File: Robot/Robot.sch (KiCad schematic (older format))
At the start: 29 parts, among them Q1 NPN, U1 MENC, U2 MENC

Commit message: Dodani nekateri elementi na shemi
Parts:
- added C?: C, symbol C
- added D?: LED, symbol LED
- added Q?: Q_PMOS_GDS, symbol Q_PMOS_GDS
- added R? (x3): 10k, symbol R
- added R?: 150, symbol R
- added SW?: SPDT_Switch, symbol SPDT_Switch
- Q1: value NPN -> NPN B=100
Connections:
- net labels added: BATVOL, LEDBAT
- wire segments 166 -> 189
- no-connect marks 12 -> 11
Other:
- note added: "Z LED lučko prikazujemo napetost na bateriji."
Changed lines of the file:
@@
 U 1 1 58BBD1F6
 P 2450 1300
-F 0 "BT1" H 2550 1400 50  0000 L CNN
-F 1 "Baterija 9V" H 2550 1300 50  0000 L CNN
+F 0 "BT1" V 2200 1350 50  0000 L CNN
+F 1 "Baterija 9V" V 2300 1200 50  0000 L CNN
 F 2 "" V 2450 1360 50  0000 C CNN
 F 3 "" V 2450 1360 50  0000 C CNN
@@
 L +9V #PWR3
 U 1 1 58BBD76D
-P 2450 1100
-F 0 "#PWR3" H 2450 950 50  0001 C CNN
-F 1 "+9V" H 2450 1240 50  0000 C CNN
-F 2 "" H 2450 1100 50  0000 C CNN
-F 3 "" H 2450 1100 50  0000 C CNN
-	1    2450 1100
+P 2450 1000
+F 0 "#PWR3" H 2450 850 50  0001 C CNN
+F 1 "+9V" H 2450 1140 50  0000 C CNN
+F 2 "" H 2450 1000 50  0000 C CNN
+F 3 "" H 2450 1000 50  0000 C CNN
+	1    2450 1000
 	1    0    0    -1
 $EndComp
@@
 L GND #PWR4
 U 1 1 58BC083D
-P 2450 1400
-F 0 "#PWR4" H 2450 1150 50  0001 C CNN
-F 1 "GND" H 2450 1250 50  0000 C CNN
-F 2 "" H 2450 1400 50  0000 C CNN
-F 3 "" H 2450 1400 50  0000 C CNN
-	1    2450 1400
+P 2450 1750
+F 0 "#PWR4" H 2450 1500 50  0001 C CNN
+F 1 "GND" H 2450 1600 50  0000 C CNN
+F 2 "" H 2450 1750 50  0000 C CNN
+F 3 "" H 2450 1750 50  0000 C CNN
+	1    2450 1750
 	1    0    0    -1
 $EndComp
@@
 P 4250 8900
 F 0 "Q1" H 4450 8950 50  0000 L CNN
-F 1 "NPN" H 4450 8850 50  0000 L CNN
+F 1 "NPN B=100" H 4450 8850 50  0000 L CNN
 F 2 "" H 4450 9000 50  0000 C CNN
 F 3 "" H 4250 8900 50  0000 C CNN
@@
 	6300 1750 6400 1850
 NoConn ~ 8950 1950
-NoConn ~ 8950 2050
-NoConn ~ 8950 2150
 Entry Wire Line
 	9950 2750 10050 2850
@@
 Text Label 6600 2050 0    60   ~ 0
 AIN1
-Text Label 6600 1850 0    60   ~ 0
-AIN2
 Text Label 6600 1750 0    60   ~ 0
 AOUTL
@@
 Wire Wire Line
 	8950 2350 9350 2350
+$Comp
+L C C?
+U 1 1 58C5CD2F
+P 2800 1250
+F 0 "C?" H 2825 1350 50  0000 L CNN
+F 1 "C" H 2825 1150 50  0000 L CNN
+F 2 "" H 2838 1100 50  0000 C CNN
+F 3 "" H 2800 1250 50  0000 C CNN
+	1    2800 1250
+	1    0    0    -1
+$EndComp
+Wire Wire Line
+	2450 1100 2450 1000
+Wire Wire Line
+	2450 1400 2450 1750
+Wire Wire Line
+	2800 1400 2450 1400
+NoConn ~ 8950 2550
+Connection ~ 2800 1100
+$Comp
+L R R?
+U 1 1 58C66BFC
+P 4150 1250
+F 0 "R?" V 4230 1250 50  0000 C CNN
+F 1 "10k" V 4150 1250 50  0000 C CNN
+F 2 "" V 4080 1250 50  0000 C CNN
+F 3 "" H 4150 1250 50  0000 C CNN
+	1    4150 1250
+	1    0    0    -1
+$EndComp
+Wire Wire Line
+	2450 1100 4600 1100
+Wire Wire Line
+	3800 1400 4300 1400
+$Comp
+L SPDT_Switch SW?
+U 1 1 58C6748C
+P 3400 1600
+F 0 "SW?" H 3350 1850 60  0000 C CNN
+F 1 "SPDT_Switch" H 3350 1350 60  0000 C CNN
+F 2 "" H 3400 1600 60  0001 C CNN
+F 3 "" H 3400 1600 60  0001 C CNN
+	1    3400 1600
+	1    0    0    -1
+$EndComp
+Wire Wire Line
+	3050 1750 2800 1750
+Wire Wire Line
+	2800 1750 2800 1400
+Wire Wire Line
+	3050 1450 3050 1100
+Connection ~ 3050 1100
+Wire Wire Line
+	3800 1400 3800 1600
+$Comp
+L Q_PMOS_GDS Q?
+U 1 1 58C67B7D
+P 4500 1700
+F 0 "Q?" H 4700 1750 50  0000 L CNN
+F 1 "Q_PMOS_GDS" H 4700 1650 50  0000 L CNN
+F 2 "" H 4700 1800 50  0000 C CNN
+F 3 "" H 4500 1700 50  0000 C CNN
+	1    4500 1700
+	1    0    0    -1
+$EndComp
+Wire Wire Line
+	4300 1400 4300 1700
+Connection ~ 4150 1400
+Wire Wire Line
+	4600 1100 4600 1500
+Connection ~ 4150 1100
+Wire Wire Line
+	4600 1900 4600 2000
+Wire Wire Line
+	4600 2000 5450 2000
+Wire Wire Line
+	5450 2000 5450 1800
+$Comp
+L +9V #PWR?
+U 1 1 58C67FC0
+P 5450 1800
+F 0 "#PWR?" H 5450 1650 50  0001 C CNN
+F 1 "+9V" H 5450 1940 50  0000 C CNN
+F 2 "" H 5450 1800 50  0000 C CNN
+F 3 "" H 5450 1800 50  0000 C CNN
+	1    5450 1800
+	1    0    0    -1
+$EndComp
+$Comp
+L R R?
+U 1 1 58C6804F
+P 5450 2150
+F 0 "R?" V 5530 2150 50  0000 C CNN
+F 1 "10k" V 5450 2150 50  0000 C CNN
+F 2 "" V 5380 2150 50  0000 C CNN
+F 3 "" H 5450 2150 50  0000 C CNN
+	1    5450 2150
+	1    0    0    -1
+$EndComp
+$Comp
+L R R?
+U 1 1 58C680E1
+P 5450 2550
+F 0 "R?" V 5530 2550 50  0000 C CNN
+F 1 "10k" V 5450 2550 50  0000 C CNN
+F 2 "" V 5380 2550 50  0000 C CNN
+F 3 "" H 5450 2550 50  0000 C CNN
+	1    5450 2550
+	1    0    0    -1
+$EndComp
+Wire Wire Line
+	5450 2300 5450 2400
+$Comp
+L GND #PWR?
+U 1 1 58C6828F
+P 5450 2700
+F 0 "#PWR?" H 5450 2450 50  0001 C CNN
+F 1 "GND" H 5450 2550 50  0000 C CNN
+F 2 "" H 5450 2700 50  0000 C CNN
+F 3 "" H 5450 2700 50  0000 C CNN
+	1    5450 2700
+	1    0    0    -1
+$EndComp
+Wire Wire Line
+	5450 2350 4800 2350
+Wire Wire Line
+	4800 2350 4800 3000
+Connection ~ 5450 2350
+Entry Wire Line
+	4800 3000 4900 3100
+Text Label 4950 2350 0    60   ~ 0
+BATVOL
+Wire Wire Line
+	8950 2150 9950 2150
+Entry Wire Line
+	9950 2150 10050 2250
+Text Label 9050 2150 0    60   ~ 0
+BATVOL
+Wire Wire Line
+	8950 2050 9950 2050
+Entry Wire Line
+	9950 2050 10050 2150
+Text Label 9050 2050 0    60   ~ 0
+AIN2
+Text Label 6600 1850 0    60   ~ 0
+LEDBAT
+$Comp
+L LED D?
+U 1 1 58C6B057
+P 11350 1550
+F 0 "D?" H 11350 1650 50  0000 C CNN
+F 1 "LED" H 11350 1450 50  0000 C CNN
+F 2 "" H 11350 1550 50  0000 C CNN
+F 3 "" H 11350 1550 50  0000 C CNN
+	1    11350 1550
+	-1   0    0    1
+$EndComp
+Entry Wire Line
+	10050 1450 10150 1550
+Wire Wire Line
+	10150 1550 11200 1550
+$Comp
+L R R?
+U 1 1 58C6BA8C
+P 11900 1550
+F 0 "R?" V 11980 1550 50  0000 C CNN
+F 1 "150" V 11900 1550 50  0000 C CNN
+F 2 "" V 11830 1550 50  0000 C CNN
+F 3 "" H 11900 1550 50  0000 C CNN
+	1    11900 1550
+	0    1    1    0
+$EndComp
+Wire Wire Line
+	11500 1550 11750 1550
+Wire Wire Line
+	12050 1550 12600 1550
+Wire Wire Line
+	12600 1550 12600 1700
+$Comp
+L GND #PWR?
+U 1 1 58C6BDA7
+P 12600 1700
+F 0 "#PWR?" H 12600 1450 50  0001 C CNN
+F 1 "GND" H 12600 1550 50  0000 C CNN
+F 2 "" H 12600 1700 50  0000 C CNN
+F 3 "" H 12600 1700 50  0000 C CNN
+	1    12600 1700
+	1    0    0    -1
+$EndComp
+Text Label 10450 1550 0    60   ~ 0
+LEDBAT
+Text Notes 11200 1350 0    60   ~ 0
+Z LED lučko prikazujemo napetost na bateriji.
 $EndSCHEMATC

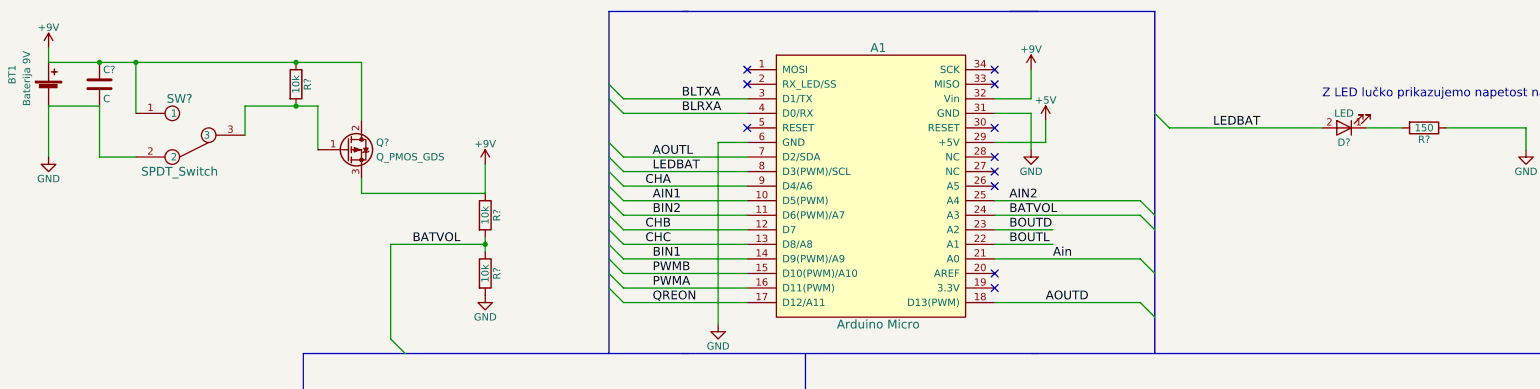
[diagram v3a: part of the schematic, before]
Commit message: Popravljena shema
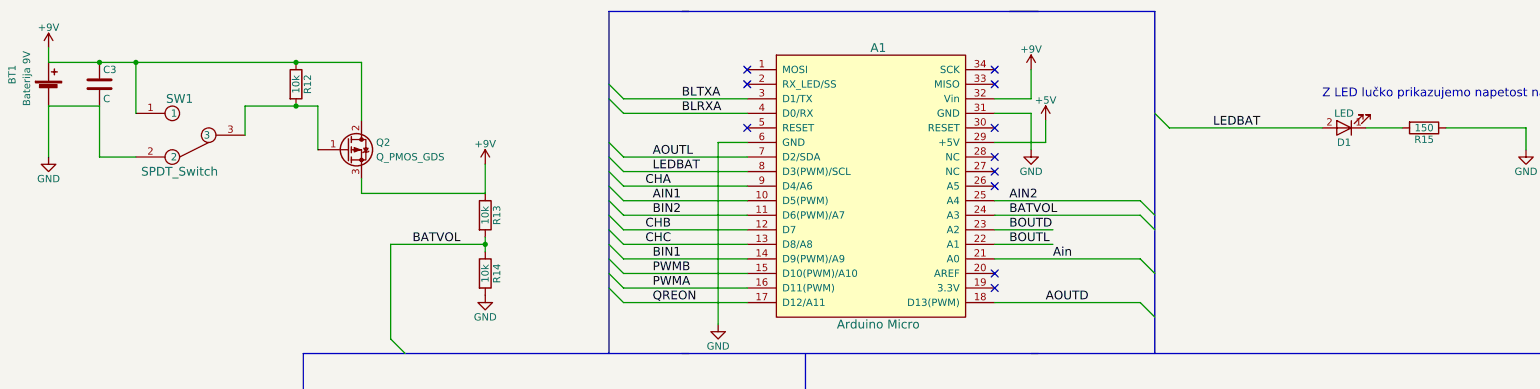
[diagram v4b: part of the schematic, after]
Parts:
- gave numbers to parts that had none: 8
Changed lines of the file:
@@
 $EndComp
 $Comp
-L GND #PWR9
+L GND #PWR11
 U 1 1 58BC1A56
 P 7000 10050
-F 0 "#PWR9" H 7000 9800 50  0001 C CNN
+F 0 "#PWR11" H 7000 9800 50  0001 C CNN
 F 1 "GND" H 7000 9900 50  0000 C CNN
 F 2 "" H 7000 10050 50  0000 C CNN
@@
 $EndComp
 $Comp
-L GND #PWR16
+L GND #PWR18
 U 1 1 58BC1E52
 P 9200 1700
-F 0 "#PWR16" H 9200 1450 50  0001 C CNN
+F 0 "#PWR18" H 9200 1450 50  0001 C CNN
 F 1 "GND" H 9200 1550 50  0000 C CNN
 F 2 "" H 9200 1700 50  0000 C CNN
@@
 $EndComp
 $Comp
-L +9V #PWR15
+L +9V #PWR17
 U 1 1 58BC1EB1
 P 9200 1150
-F 0 "#PWR15" H 9200 1000 50  0001 C CNN
+F 0 "#PWR17" H 9200 1000 50  0001 C CNN
 F 1 "+9V" H 9200 1290 50  0000 C CNN
 F 2 "" H 9200 1150 50  0000 C CNN
@@
 $EndComp
 $Comp
-L +5V #PWR17
+L +5V #PWR19
 U 1 1 58BC1EDB
 P 9300 1500
-F 0 "#PWR17" H 9300 1350 50  0001 C CNN
+F 0 "#PWR19" H 9300 1350 50  0001 C CNN
 F 1 "+5V" H 9300 1640 50  0000 C CNN
 F 2 "" H 9300 1500 50  0000 C CNN
@@
 $EndComp
 $Comp
-L GND #PWR10
+L GND #PWR12
 U 1 1 58BC1F3F
 P 7050 2900
-F 0 "#PWR10" H 7050 2650 50  0001 C CNN
+F 0 "#PWR12" H 7050 2650 50  0001 C CNN
 F 1 "GND" H 7050 2750 50  0000 C CNN
 F 2 "" H 7050 2900 50  0000 C CNN
@@
 $EndComp
 $Comp
-L +5V #PWR11
+L +5V #PWR13
 U 1 1 58BC95B9
 P 7100 4450
-F 0 "#PWR11" H 7100 4300 50  0001 C CNN
+F 0 "#PWR13" H 7100 4300 50  0001 C CNN
 F 1 "+5V" H 7100 4590 50  0000 C CNN
 F 2 "" H 7100 4450 50  0000 C CNN
@@
 $EndComp
 $Comp
-L GND #PWR8
+L GND #PWR10
 U 1 1 58BD222C
 P 6750 7950
-F 0 "#PWR8" H 6750 7700 50  0001 C CNN
+F 0 "#PWR10" H 6750 7700 50  0001 C CNN
 F 1 "GND" H 6750 7800 50  0000 C CNN
 F 2 "" H 6750 7950 50  0000 C CNN
@@
 S4
 $Comp
-L +5V #PWR14
+L +5V #PWR16
 U 1 1 58BD4C14
 P 8300 9100
-F 0 "#PWR14" H 8300 8950 50  0001 C CNN
+F 0 "#PWR16" H 8300 8950 50  0001 C CNN
 F 1 "+5V" H 8300 9240 50  0000 C CNN
 F 2 "" H 8300 9100 50  0000 C CNN
@@
 BLRXA
 $Comp
-L GND #PWR13
+L GND #PWR15
 U 1 1 58BDD562
 P 8150 4350
-F 0 "#PWR13" H 8150 4100 50  0001 C CNN
+F 0 "#PWR15" H 8150 4100 50  0001 C CNN
 F 1 "GND" H 8150 4200 50  0000 C CNN
 F 2 "" H 8150 4350 50  0000 C CNN
@@
 $EndComp
 $Comp
-L +5V #PWR12
+L +5V #PWR14
 U 1 1 58BDD71C
 P 7900 4300
-F 0 "#PWR12" H 7900 4150 50  0001 C CNN
+F 0 "#PWR14" H 7900 4150 50  0001 C CNN
 F 1 "+5V" H 7900 4440 50  0000 C CNN
 F 2 "" H 7900 4300 50  0000 C CNN
@@
 $EndComp
 $Comp
-L +9V #PWR23
+L +9V #PWR26
 U 1 1 58BDF7BA
 P 13250 4400
-F 0 "#PWR23" H 13250 4250 50  0001 C CNN
+F 0 "#PWR26" H 13250 4250 50  0001 C CNN
 F 1 "+9V" H 13250 4540 50  0000 C CNN
 F 2 "" H 13250 4400 50  0000 C CNN
@@
 $EndComp
 $Comp
-L GND #PWR24
+L GND #PWR27
 U 1 1 58BDF8AC
 P 13500 5850
-F 0 "#PWR24" H 13500 5600 50  0001 C CNN
+F 0 "#PWR27" H 13500 5600 50  0001 C CNN
 F 1 "GND" H 13500 5700 50  0000 C CNN
 F 2 "" H 13500 5850 50  0000 C CNN
@@
 $EndComp
 $Comp
-L +5V #PWR20
+L +5V #PWR22
 U 1 1 58BE122F
 P 11000 5500
-F 0 "#PWR20" H 11000 5350 50  0001 C CNN
+F 0 "#PWR22" H 11000 5350 50  0001 C CNN
 F 1 "+5V" H 11000 5640 50  0000 C CNN
 F 2 "" H 11000 5500 50  0000 C CNN
@@
 $EndComp
 $Comp
-L +5V #PWR18
+L +5V #PWR20
 U 1 1 58BE1351
 P 10750 3900
-F 0 "#PWR18" H 10750 3750 50  0001 C CNN
+F 0 "#PWR20" H 10750 3750 50  0001 C CNN
 F 1 "+5V" H 10750 4040 50  0000 C CNN
 F 2 "" H 10750 3900 50  0000 C CNN
@@
 $EndComp
 $Comp
-L GND #PWR21
+L GND #PWR23
 U 1 1 58BE1697
 P 11000 6300
-F 0 "#PWR21" H 11000 6050 50  0001 C CNN
+F 0 "#PWR23" H 11000 6050 50  0001 C CNN
 F 1 "GND" H 11000 6150 50  0000 C CNN
 F 2 "" H 11000 6300 50  0000 C CNN
@@
 $EndComp
 $Comp
-L GND #PWR19
+L GND #PWR21
 U 1 1 58BE16E1
 P 10750 4750
-F 0 "#PWR19" H 10750 4500 50  0001 C CNN
+F 0 "#PWR21" H 10750 4500 50  0001 C CNN
 F 1 "GND" H 10750 4600 50  0000 C CNN
 F 2 "" H 10750 4750 50  0000 C CNN
@@
 $EndComp
 $Comp
-L GND #PWR22
+L GND #PWR24
 U 1 1 58BE195D
 P 11850 4250
-F 0 "#PWR22" H 11850 4000 50  0001 C CNN
+F 0 "#PWR24" H 11850 4000 50  0001 C CNN
 F 1 "GND" H 11850 4100 50  0000 C CNN
 F 2 "" H 11850 4250 50  0000 C CNN
@@
 $EndComp
 $Comp
-L +5V #PWR25
+L +5V #PWR28
 U 1 1 58BE1A8C
 P 13550 4400
-F 0 "#PWR25" H 13550 4250 50  0001 C CNN
+F 0 "#PWR28" H 13550 4250 50  0001 C CNN
 F 1 "+5V" H 13550 4540 50  0000 C CNN
 F 2 "" H 13550 4400 50  0000 C CNN
@@
 	8950 2350 9350 2350
 $Comp
-L C C?
+L C C3
 U 1 1 58C5CD2F
 P 2800 1250
-F 0 "C?" H 2825 1350 50  0000 L CNN
+F 0 "C3" H 2825 1350 50  0000 L CNN
 F 1 "C" H 2825 1150 50  0000 L CNN
 F 2 "" H 2838 1100 50  0000 C CNN
@@
 Connection ~ 2800 1100
 $Comp
-L R R?
+L R R12
 U 1 1 58C66BFC
 P 4150 1250
-F 0 "R?" V 4230 1250 50  0000 C CNN
+F 0 "R12" V 4230 1250 50  0000 C CNN
 F 1 "10k" V 4150 1250 50  0000 C CNN
 F 2 "" V 4080 1250 50  0000 C CNN
@@
 	3800 1400 4300 1400
 $Comp
-L SPDT_Switch SW?
+L SPDT_Switch SW1
 U 1 1 58C6748C
 P 3400 1600
-F 0 "SW?" H 3350 1850 60  0000 C CNN
+F 0 "SW1" H 3350 1850 60  0000 C CNN
 F 1 "SPDT_Switch" H 3350 1350 60  0000 C CNN
 F 2 "" H 3400 1600 60  0001 C CNN
@@
 	3800 1400 3800 1600
 $Comp
-L Q_PMOS_GDS Q?
+L Q_PMOS_GDS Q2
 U 1 1 58C67B7D
 P 4500 1700
-F 0 "Q?" H 4700 1750 50  0000 L CNN
+F 0 "Q2" H 4700 1750 50  0000 L CNN
 F 1 "Q_PMOS_GDS" H 4700 1650 50  0000 L CNN
 F 2 "" H 4700 1800 50  0000 C CNN
@@
 	5450 2000 5450 1800
 $Comp
-L +9V #PWR?
+L +9V #PWR8
 U 1 1 58C67FC0
 P 5450 1800
-F 0 "#PWR?" H 5450 1650 50  0001 C CNN
+F 0 "#PWR8" H 5450 1650 50  0001 C CNN
 F 1 "+9V" H 5450 1940 50  0000 C CNN
 F 2 "" H 5450 1800 50  0000 C CNN
@@
 $EndComp
 $Comp
-L R R?
+L R R13
 U 1 1 58C6804F
 P 5450 2150
-F 0 "R?" V 5530 2150 50  0000 C CNN
+F 0 "R13" V 5530 2150 50  0000 C CNN
 F 1 "10k" V 5450 2150 50  0000 C CNN
 F 2 "" V 5380 2150 50  0000 C CNN
@@
 $EndComp
 $Comp
-L R R?
+L R R14
 U 1 1 58C680E1
 P 5450 2550
-F 0 "R?" V 5530 2550 50  0000 C CNN
+F 0 "R14" V 5530 2550 50  0000 C CNN
 F 1 "10k" V 5450 2550 50  0000 C CNN
 F 2 "" V 5380 2550 50  0000 C CNN
@@
 	5450 2300 5450 2400
 $Comp
-L GND #PWR?
+L GND #PWR9
 U 1 1 58C6828F
 P 5450 2700
-F 0 "#PWR?" H 5450 2450 50  0001 C CNN
+F 0 "#PWR9" H 5450 2450 50  0001 C CNN
 F 1 "GND" H 5450 2550 50  0000 C CNN
 F 2 "" H 5450 2700 50  0000 C CNN
@@
 LEDBAT
 $Comp
-L LED D?
+L LED D1
 U 1 1 58C6B057
 P 11350 1550
-F 0 "D?" H 11350 1650 50  0000 C CNN
+F 0 "D1" H 11350 1650 50  0000 C CNN
 F 1 "LED" H 11350 1450 50  0000 C CNN
 F 2 "" H 11350 1550 50  0000 C CNN
@@
 	10150 1550 11200 1550
 $Comp
-L R R?
+L R R15
 U 1 1 58C6BA8C
 P 11900 1550
-F 0 "R?" V 11980 1550 50  0000 C CNN
+F 0 "R15" V 11980 1550 50  0000 C CNN
 F 1 "150" V 11900 1550 50  0000 C CNN
 F 2 "" V 11830 1550 50  0000 C CNN
@@
 	12600 1550 12600 1700
 $Comp
-L GND #PWR?
+L GND #PWR25
 U 1 1 58C6BDA7
 P 12600 1700
-F 0 "#PWR?" H 12600 1450 50  0001 C CNN
+F 0 "#PWR25" H 12600 1450 50  0001 C CNN
 F 1 "GND" H 12600 1550 50  0000 C CNN
 F 2 "" H 12600 1700 50  0000 C CNN
